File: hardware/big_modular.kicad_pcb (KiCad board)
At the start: 2 copper layers, 100.5 x 60 mm, 5 parts, among them J1 USB4105-GF-A

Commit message: WIP: consolidate PD-only Eurorack circuit on one sheet and dimension 2HP assembly
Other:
- board text added: "2 machined corner blocks: see ../docs/assembly.svg"
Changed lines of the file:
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@@
-	(footprint ""
-		(layer "F.Cu")
-		(at 80.75 52.275)
-		(property "Reference" "H3"
-			(at 0 0 0)
-			(layer "F.SilkS")
-			(hide yes)
-			(effects
-				(font
-					(size 1.27 1.27)
-				)
-			)
-		)
-		(property "Value" "MECHANICAL_NPTH"
-			(at 0 0 0)
-			(layer "F.Fab")
-			(hide yes)
-			(effects
-				(font
-					(size 1.27 1.27)
-				)
-			)
-		)
-		(property "Datasheet" ""
-			(at 0 0 0)
-			(layer "F.Fab")
-			(hide yes)
-			(effects
-				(font
-					(size 1.27 1.27)
-				)
-			)
-		)
-		(property "Description" ""
-			(at 0 0 0)
-			(layer "F.Fab")
-			(hide yes)
-			(effects
-				(font
-					(size 1.27 1.27)
-				)
-			)
-		)
-		(duplicate_pad_numbers_are_jumpers no)
-		(pad "" np_thru_hole circle
-			(at 0 0)
-			(size 2.2 2.2)
-			(drill 2.2)
-			(layers "*.Cu")
-		)
-		(embedded_fonts no)
-	)
-	(footprint ""
-		(layer "F.Cu")
-		(at 119.25 98.275)
-		(property "Reference" "H2"
-			(at 0 0 0)
-			(layer "F.SilkS")
-			(hide yes)
-			(effects
-				(font
-					(size 1.27 1.27)
-				)
-			)
-		)
-		(property "Value" "MECHANICAL_NPTH"
-			(at 0 0 0)
-			(layer "F.Fab")
-			(hide yes)
-			(effects
-				(font
-					(size 1.27 1.27)
-				)
-			)
-		)
-		(property "Datasheet" ""
-			(at 0 0 0)
-			(layer "F.Fab")
-			(hide yes)
-			(effects
-				(font
-					(size 1.27 1.27)
-				)
-			)
-		)
-		(property "Description" ""
-			(at 0 0 0)
-			(layer "F.Fab")
-			(hide yes)
-			(effects
-				(font
-					(size 1.27 1.27)
-				)
-			)
-		)
-		(duplicate_pad_numbers_are_jumpers no)
-		(pad "" np_thru_hole circle
-			(at 0 0)
-			(size 2.2 2.2)
-			(drill 2.2)
-			(layers "*.Cu")
-		)
-		(embedded_fonts no)
-	)
 	(footprint ""
 		(layer "F.Cu")
@@
 	(footprint ""
 		(layer "F.Cu")
-		(at 119.25 52.275)
-		(property "Reference" "H4"
+		(at 80.75 52.275)
+		(property "Reference" "H3"
 			(at 0 0 0)
 			(layer "F.SilkS")
@@
 		(embedded_fonts no)
 	)
+	(footprint ""
+		(layer "F.Cu")
+		(at 119.25 52.275)
+		(property "Reference" "H4"
+			(at 0 0 0)
+			(layer "F.SilkS")
+			(hide yes)
+			(effects
+				(font
+					(size 1.27 1.27)
+				)
+			)
+		)
+		(property "Value" "MECHANICAL_NPTH"
+			(at 0 0 0)
+			(layer "F.Fab")
+			(hide yes)
+			(effects
+				(font
+					(size 1.27 1.27)
+				)
+			)
+		)
+		(property "Datasheet" ""
+			(at 0 0 0)
+			(layer "F.Fab")
+			(hide yes)
+			(effects
+				(font
+					(size 1.27 1.27)
+				)
+			)
+		)
+		(property "Description" ""
+			(at 0 0 0)
+			(layer "F.Fab")
+			(hide yes)
+			(effects
+				(font
+					(size 1.27 1.27)
+				)
+			)
+		)
+		(duplicate_pad_numbers_are_jumpers no)
+		(pad "" np_thru_hole circle
+			(at 0 0)
+			(size 2.2 2.2)
+			(drill 2.2)
+			(layers "*.Cu")
+		)
+		(embedded_fonts no)
+	)
+	(footprint ""
+		(layer "F.Cu")
+		(at 119.25 98.275)
+		(property "Reference" "H2"
+			(at 0 0 0)
+			(layer "F.SilkS")
+			(hide yes)
+			(effects
+				(font
+					(size 1.27 1.27)
+				)
+			)
+		)
+		(property "Value" "MECHANICAL_NPTH"
+			(at 0 0 0)
+			(layer "F.Fab")
+			(hide yes)
+			(effects
+				(font
+					(size 1.27 1.27)
+				)
+			)
+		)
+		(property "Datasheet" ""
+			(at 0 0 0)
+			(layer "F.Fab")
+			(hide yes)
+			(effects
+				(font
+					(size 1.27 1.27)
+				)
+			)
+		)
+		(property "Description" ""
+			(at 0 0 0)
+			(layer "F.Fab")
+			(hide yes)
+			(effects
+				(font
+					(size 1.27 1.27)
+				)
+			)
+		)
+		(duplicate_pad_numbers_are_jumpers no)
+		(pad "" np_thru_hole circle
+			(at 0 0)
+			(size 2.2 2.2)
+			(drill 2.2)
+			(layers "*.Cu")
+		)
+		(embedded_fonts no)
+	)
+	(gr_line
+		(start 76.75 94.275)
+		(end 76.75 102.675)
+		(stroke
+			(width 0.15)
+			(type default)
+		)
+		(layer "Dwgs.User")
+	)
+	(gr_line
+		(start 76.75 102.675)
+		(end 84.75 102.675)
+		(stroke
+			(width 0.15)
+			(type default)
+		)
+		(layer "Dwgs.User")
+	)
+	(gr_line
+		(start 84.75 94.275)
+		(end 76.75 94.275)
+		(stroke
+			(width 0.15)
+			(type default)
+		)
+		(layer "Dwgs.User")
+	)
+	(gr_line
+		(start 84.75 102.675)
+		(end 84.75 94.275)
+		(stroke
+			(width 0.15)
+			(type default)
+		)
+		(layer "Dwgs.User")
+	)
 	(gr_line
 		(start 100 93)
@@
 		(start 100 101)
 		(end 100 93)
+		(stroke
+			(width 0.15)
+			(type default)
+		)
+		(layer "Dwgs.User")
+	)
+	(gr_line
+		(start 115.25 94.275)
+		(end 115.25 102.675)
+		(stroke
+			(width 0.15)
+			(type default)
+		)
+		(layer "Dwgs.User")
+	)
+	(gr_line
+		(start 115.25 102.675)
+		(end 123.25 102.675)
+		(stroke
+			(width 0.15)
+			(type default)
+		)
+		(layer "Dwgs.User")
+	)
+	(gr_line
+		(start 123.25 94.275)
+		(end 115.25 94.275)
+		(stroke
+			(width 0.15)
+			(type default)
+		)
+		(layer "Dwgs.User")
+	)
+	(gr_line
+		(start 123.25 102.675)
+		(end 123.25 94.275)
 		(stroke
 			(width 0.15)
@@
 		(layer "Dwgs.User")
 		(effects
+			(font
+				(size 0.9 0.9)
+				(thickness 0.12)
+			)
+		)
+	)
+	(gr_text "2 machined corner blocks: see ../docs/assembly.svg"
+		(at 100 117 0)
+		(layer "Dwgs.User")
+		(effects

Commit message: Update on the PCB.
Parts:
- added D10: 3mm THT LED / FORM 90 DEG, BigModular:LED_D3.0mm_Horizontal_O1.27mm_Z2.0mm_Edge, F.Cu at (72.5, 97.9)
- added J7: EURORACK OUTPUT PIGTAIL / NOT INPUT, BigModular:WireLanding_2x08_P2.54mm, F.Cu at (83.8, 77.3)
- added R32: 2.2k PROVISIONAL, BigModular:R_Axial_DIN0207_L6.3mm_D2.5mm_P7.62mm_Horizontal, F.Cu at (78.8, 90.3)
- added SW1: TL3340AF160QG, BigModular:SW_TL3340AF160QG_HandSolder, F.Cu at (126.8, 100.2)
- moved H4 28.2 mm to (106.2, 77.3)
- moved H3 25.0 mm to (79.2, 77.3)
- moved H1 24.7 mm to (57.8, 89.3)
- moved H2 24.7 mm to (142.2, 89.3)
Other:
- board size 100.5 x 60 mm -> 100.5 x 30 mm
- board text added: "1 / -12V / RED"
- board text added: "A4.2 / MAIN PCB / TWO-BOARD PLACEMENT / NO ROUTING"
- board text added: "J7 -> J2 OUTPUT ONLY"
- board text added: "M3 ONLY: two bracket holes; no standoffs / no board-to-board headers"
- board text added: "PWR K"
- board text added: "R32"
- board text added: "RESET"
- board text added: "UI nets isolated; not a working reset/power indicator circuit"
- board text added: "USB + 3mm THT LED + hand-solder 90-degree SMT reset; no middle board"
- board text removed: "2 machined corner blocks: see ../docs/assembly.svg"
- board text removed: "Carrier top X=3.170; PCB bottom X=1.570"
- board text removed: "Carrier: Y=14..114.5; Z=2..62 mm"
- board text removed: "J1 MOUTH Z=+0.800 / insertion +Z / panel normal"
- board text removed: "PLACEMENT ONLY / NO ROUTING / NOT BUILDABLE"

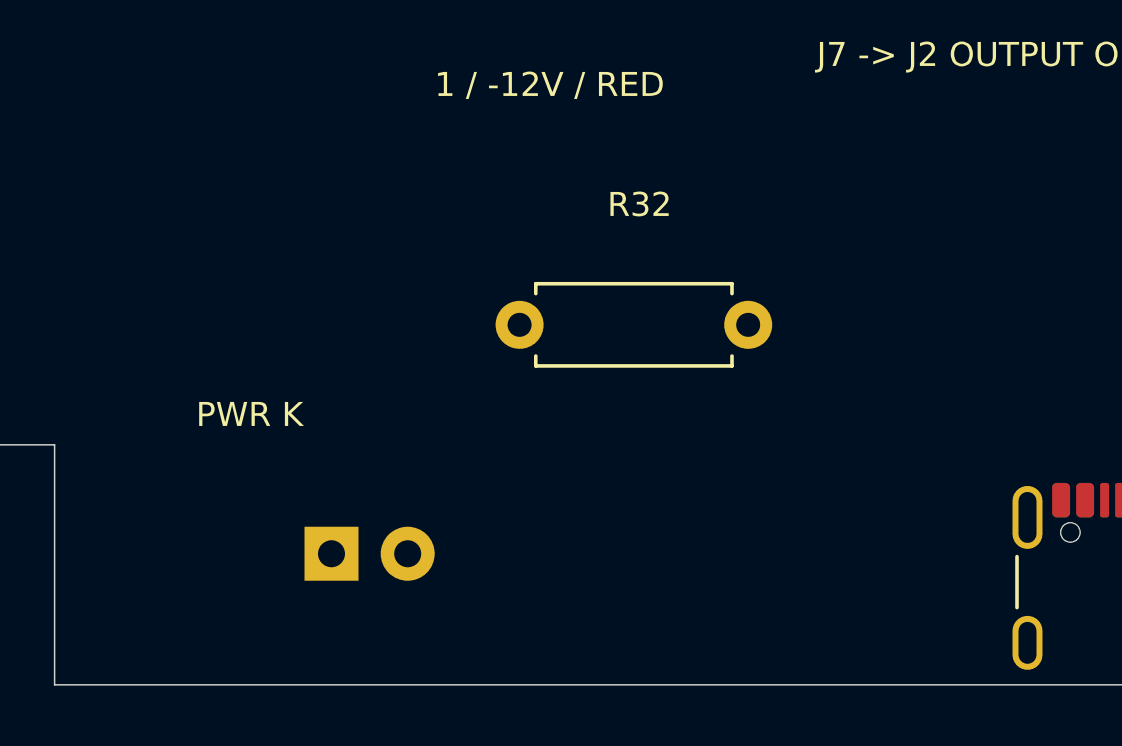
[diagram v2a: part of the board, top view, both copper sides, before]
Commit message: Save 9 V power-supply schematic prototype and LED mechanical provisions
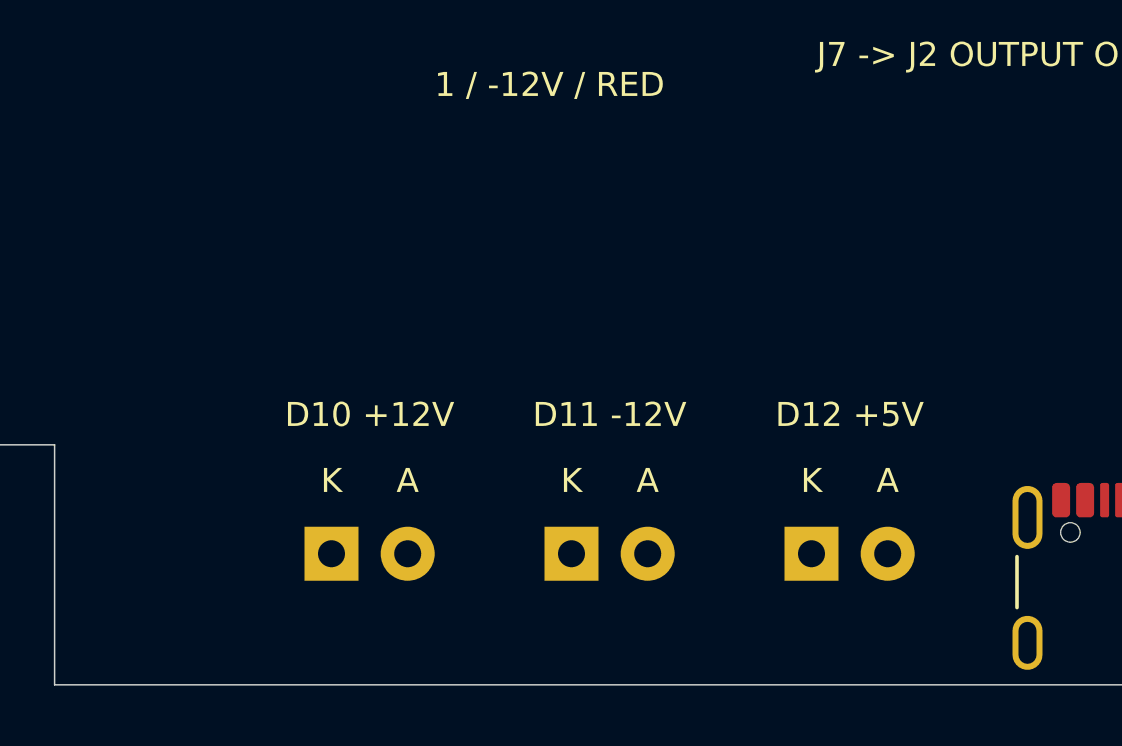
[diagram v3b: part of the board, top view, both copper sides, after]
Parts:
- removed R32: 2.2k PROVISIONAL, BigModular:R_Axial_DIN0207_L6.3mm_D2.5mm_P7.62mm_Horizontal
- added D11: RED 3mm / -12V / MANUAL, BigModular:LED_D3.0mm_Horizontal_O1.27mm_Z2.0mm_Edge, F.Cu at (80.5, 97.9)
- added D12: RED 3mm / +5V / MANUAL, BigModular:LED_D3.0mm_Horizontal_O1.27mm_Z2.0mm_Edge, F.Cu at (88.5, 97.9)
- D10: value 3mm THT LED / FORM 90 DEG -> RED 3mm / +12V / MANUAL
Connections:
- net UI_GND_PENDING renamed D10_K_PENDING
- D10 pad 2: LED_A_PENDING -> D10_A_PENDING
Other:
- board text added: "A"
- board text added: "D10 +12V"
- board text added: "D11 -12V"
- board text added: "D12 +5V"
- board text added: "K"
- board text added: "USB + 3 RED 3mm THT LEDs + hand-solder SMT reset; no middle board"
- board text removed: "PWR K"
- board text removed: "R32"
- board text removed: "USB + 3mm THT LED + hand-solder 90-degree SMT reset; no middle board"

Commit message: Replace MCU diagnostics with optional rail-sense IDC and single 5 V power LED
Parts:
- removed D11: RED 3mm / -12V / MANUAL, BigModular:LED_D3.0mm_Horizontal_O1.27mm_Z2.0mm_Edge
- removed D12: RED 3mm / +5V / MANUAL, BigModular:LED_D3.0mm_Horizontal_O1.27mm_Z2.0mm_Edge
- D10: value RED 3mm / +12V / MANUAL -> RED 3mm / +5V POWER / MANUAL
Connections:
- net D10_A_PENDING renamed LED_P_A
- D10 pad 1: D10_K_PENDING -> GND
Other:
- board text added: "D10 +5V POWER"
- board text added: "D10: final +5V via1k to anode; cathode GND; no routing"
- board text added: "USB + 1 RED 3mm THT +5V power LED + hand-solder SMT reset; no middle board"
- board text removed: "D10 +12V"
- board text removed: "D11 -12V"
- board text removed: "D12 +5V"
- board text removed: "UI nets isolated; not a working reset/power indicator circuit"
- board text removed: "USB + 3 RED 3mm THT LEDs + hand-solder SMT reset; no middle board"

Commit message: Move USB, retry button and power LED to top; synchronize 64 V1 footprints without routing
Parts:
- added C1: 1u 50V X7R, BigModular:C_0805_2012Metric, F.Cu at (170.0, 75.0)
- added C10: 6.8p 50V C0G, BigModular:C_0603_1608Metric, F.Cu at (188.0, 75.0)
- added C11: 6.8p 50V C0G, BigModular:C_0603_1608Metric, F.Cu at (206.0, 75.0)
- added C12: 220n 50V X7R, BigModular:C_0603_1608Metric, F.Cu at (224.0, 75.0)
- added C13: 10n 50V X7R, BigModular:C_0603_1608Metric, F.Cu at (242.0, 75.0)
- added C14: 4.7n 50V C0G, BigModular:C_0603_1608Metric, F.Cu at (260.0, 75.0)
- added C15: 100n 50V X7R, BigModular:C_0603_1608Metric, F.Cu at (278.0, 75.0)
- added C16: 10u 25V X7R, BigModular:C_1206_3216Metric, F.Cu at (296.0, 75.0)
- added C17: 10u 25V X7R, BigModular:C_1206_3216Metric, F.Cu at (314.0, 75.0)
- added C18: 10u 25V X7R, BigModular:C_1206_3216Metric, F.Cu at (332.0, 75.0)
- added C19: 22u 25V X7R, BigModular:C_1210_3225Metric, F.Cu at (170.0, 93.0)
- added C2: 100n 50V X7R, BigModular:C_0603_1608Metric, F.Cu at (188.0, 93.0)
- added C20: 100n 50V X7R, BigModular:C_0603_1608Metric, F.Cu at (206.0, 93.0)
- added C3: 100n 50V X7R, BigModular:C_0603_1608Metric, F.Cu at (224.0, 93.0)
- added C35: 100n 50V X7R, BigModular:C_0603_1608Metric, F.Cu at (242.0, 93.0)
- added C36: 100n 50V X7R, BigModular:C_0603_1608Metric, F.Cu at (260.0, 93.0)
- added C37: 22u 25V X7R, BigModular:C_1210_3225Metric, F.Cu at (278.0, 93.0)
- added C38: 22u 25V X7R, BigModular:C_1210_3225Metric, F.Cu at (296.0, 93.0)
- added C4: 10u 25V X7R, BigModular:C_1206_3216Metric, F.Cu at (314.0, 93.0)
- added C5: 10u 25V X7R, BigModular:C_1206_3216Metric, F.Cu at (332.0, 93.0)
- added C6: 22u 25V X7R, BigModular:C_1210_3225Metric, F.Cu at (170.0, 111.0)
- added C7: 100n 50V X7R, BigModular:C_0603_1608Metric, F.Cu at (188.0, 111.0)
- added C8: 22u 25V X7R, BigModular:C_1210_3225Metric, F.Cu at (206.0, 111.0)
- added C9: 22u 25V X7R, BigModular:C_1210_3225Metric, F.Cu at (224.0, 111.0)
- added D2: SS34 40V, BigModular:D_SMA, F.Cu at (242.0, 111.0)
- added D3: SS34 40V, BigModular:D_SMA, F.Cu at (260.0, 111.0)
- added F1: 3A 32V candidate, BigModular:Fuse_1206_3216Metric, F.Cu at (278.0, 111.0)
- added L1: 6.8uH 20% shielded, BigModular:L_KOHER_MDA1040, F.Cu at (296.0, 111.0)
- added L2: 4.7uH 20% shielded, BigModular:L_CENKER_CKCS6045, F.Cu at (314.0, 111.0)
- added L3: 4.7uH 20% shielded, BigModular:L_CENKER_CKCS6045, F.Cu at (332.0, 111.0)
- added L4: 6.8uH 20% shielded, BigModular:L_KOHER_MDA1040, F.Cu at (170.0, 129.0)
- added R10: 12.9k 0.1%, BigModular:R_0603_1608Metric, F.Cu at (188.0, 129.0)
- added R12: 1.33M 1%, BigModular:R_0603_1608Metric, F.Cu at (206.0, 129.0)
- added R13: 150k 1%, BigModular:R_0603_1608Metric, F.Cu at (224.0, 129.0)
- added R14: 1.33M 1%, BigModular:R_0603_1608Metric, F.Cu at (242.0, 129.0)
- added R15: 150k 1%, BigModular:R_0603_1608Metric, F.Cu at (260.0, 129.0)
- added R16: 100 1%, BigModular:R_0603_1608Metric, F.Cu at (278.0, 129.0)
- added R17: 100k 1%, BigModular:R_0603_1608Metric, F.Cu at (296.0, 129.0)
- added R18: 13.5k 0.1%, BigModular:R_0603_1608Metric, F.Cu at (314.0, 129.0)
- added R2: 6.8k 1%, BigModular:R_0603_1608Metric, F.Cu at (332.0, 129.0)
- added R25: 10k 1%, BigModular:R_0603_1608Metric, F.Cu at (170.0, 147.0)
- added R26: 10k 1%, BigModular:R_0603_1608Metric, F.Cu at (188.0, 147.0)
- added R27: 10k 1%, BigModular:R_0603_1608Metric, F.Cu at (206.0, 147.0)
- added R31: 10k 1%, BigModular:R_0603_1608Metric, F.Cu at (224.0, 147.0)
- added R32: 1k 1%, BigModular:R_0603_1608Metric, F.Cu at (242.0, 147.0)
- added R36: 402k 1%, BigModular:R_0603_1608Metric, F.Cu at (260.0, 147.0)
- added R38: 100k 1%, BigModular:R_0603_1608Metric, F.Cu at (278.0, 147.0)
- added R4: 562k 1%, BigModular:R_0603_1608Metric, F.Cu at (296.0, 147.0)
- added R40: 100k 1%, BigModular:R_0603_1608Metric, F.Cu at (314.0, 147.0)
- added R5: 100k 1%, BigModular:R_0603_1608Metric, F.Cu at (332.0, 147.0)
- added R6: 806k 1%, BigModular:R_0603_1608Metric, F.Cu at (170.0, 165.0)
- added R60: 150k 1%, BigModular:R_0603_1608Metric, F.Cu at (188.0, 165.0)
- added R7: 100k 1%, BigModular:R_0603_1608Metric, F.Cu at (206.0, 165.0)
- added R8: 6.04k 1%, BigModular:R_0603_1608Metric, F.Cu at (224.0, 165.0)
- added R9: 100k 0.1%, BigModular:R_0603_1608Metric, F.Cu at (242.0, 165.0)
- added U1: CH224A, BigModular:SSOP-10-1EP_3.9x4.9mm_P1mm_EP2.1x3.3mm, F.Cu at (260.0, 165.0)
- added U2: TPS26600PWPR, BigModular:HTSSOP-16-1EP_4.4x5mm_P0.65mm_EP3.4x5mm_Mask2.66x2.46mm, F.Cu at (278.0, 165.0)
- added U3: TPS54302DDCR, BigModular:SOT-23-6, F.Cu at (296.0, 165.0)
- added U4: TPS65131RGER, BigModular:Texas_RGE0024B_VQFN-24-1EP_4x4mm_P0.5mm_EP2.45x2.45mm, F.Cu at (314.0, 165.0)
- added U5: TPS54302DDCR, BigModular:SOT-23-6, F.Cu at (332.0, 165.0)
- J7: value EURORACK OUTPUT PIGTAIL / NOT INPUT -> Manual IDC wire landing
- moved SW1 48.0 mm to (78.8, 100.2)
- moved J1 30.8 mm to (69.2, 99.8)
- moved D10 11.5 mm to (84.0, 97.9)
- renumbered H2 to ?, H3 to ?, H1 to ?, H4 to ?
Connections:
- net GND renamed /GND
- net N12 renamed /N12
- net P12 renamed /P12
- net P5 renamed /P5
- net RESET_A_PENDING renamed /Autonomous hardware window and retry/EF_SHDN
- net VBUS_RAW renamed /USB PD input/USB_VBUS
- D10 pad 2: LED_P_A -> /Board output and power LED/LED_P_A
- J1 pad A5: CC1 -> /USB PD input/CC1
- J1 pad A6: (no net) -> unconnected-(J1-D+-PadA6)
- J1 pad A7: (no net) -> unconnected-(J1-D--PadA7)
- J1 pad A8: (no net) -> unconnected-(J1-SBU1-PadA8)
- J1 pad B5: CC2 -> /USB PD input/CC2
- J1 pad B6: (no net) -> unconnected-(J1-D+-PadB6)
- J1 pad B7: (no net) -> unconnected-(J1-D--PadB7)
- J1 pad B8: (no net) -> unconnected-(J1-SBU2-PadB8)
- J7 pad 13: (no net) -> unconnected-(J7-Pin_13-Pad13)
- J7 pad 14: (no net) -> unconnected-(J7-Pin_14-Pad14)
- J7 pad 15: (no net) -> unconnected-(J7-Pin_15-Pad15)
- J7 pad 16: (no net) -> unconnected-(J7-Pin_16-Pad16)
- SW1 pad 2: RESET_B_PENDING -> /Autonomous hardware window and retry/RTN
- SW1 pad MP: (no net) -> unconnected-(SW1-CASE-PadMP)
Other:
- board text added: "J7 OUTPUT ONLY"
- board text added: "RETRY"
- board text added: "STAGED OFF-BOARD: 60 parts; place power circuits deliberately before routing"
- board text added: "V1 / 64 PARTS SYNCHRONIZED / NO ROUTING"
- board text removed: "A4.2 / MAIN PCB / TWO-BOARD PLACEMENT / NO ROUTING"
- board text removed: "J7 -> J2 OUTPUT ONLY"
- board text removed: "RESET"

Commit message: Swap retry switch and power LED positions on carrier and front panel
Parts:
- moved D10 6.50 mm to (77.5, 97.9)
- moved SW1 6.50 mm to (85.2, 100.2)
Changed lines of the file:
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@@
 		(locked yes)
 		(layer "F.Cu")
-		(at 78.75 100.175)
+		(at 85.25 100.175)
 		(descr "TL3340AF160QG, P021301 Rev B: hand-solder toe extensions, pin1+3 common; no substitution by size alone")
 		(property "Reference" "SW1"
@@
 		(locked yes)
 		(layer "F.Cu")
-		(at 83.98 97.905)
+		(at 77.48 97.905)
 		(descr "LED, diameter 3.0mm, horizontal offset 1.27mm, z-position of LED center 2.0mm, 2 pins, generated by kicad-footprint-generator")
 		(tags "LED")
@@
 		(layer "Edge.Cuts")
 	)
-	(gr_text "RETRY"
-		(at 78.75 92.275 0)
+	(gr_text "K"
+		(at 77.48 95.475 0)
 		(layer "F.SilkS")
 		(effects
@@
 		)
 	)
-	(gr_text "1 / -12V / RED"
-		(at 79.75 82.275 0)
+	(gr_text "D10 +5V POWER"
+		(at 78.75 93.275 0)
 		(layer "F.SilkS")
 		(effects
@@
 		)
 	)
-	(gr_text "K"
-		(at 83.98 95.475 0)
+	(gr_text "1 / -12V / RED"
+		(at 79.75 82.275 0)
 		(layer "F.SilkS")
 		(effects
@@
 		)
 	)
-	(gr_text "D10 +5V POWER"
-		(at 85.25 93.275 0)
+	(gr_text "A"
+		(at 80.02 95.475 0)
 		(layer "F.SilkS")
 		(effects
@@
 		)
 	)
-	(gr_text "A"
-		(at 86.52 95.475 0)
+	(gr_text "RETRY"
+		(at 85.25 92.275 0)
 		(layer "F.SilkS")
 		(effects

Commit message: Complete four-layer routing, adopt proven HRO USB-C and release checked fabrication files
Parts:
- J1: value USB4105-GF-A -> TYPE-C-31-M-12; footprint BigModular:USB_C_Receptacle_GCT_USB4105-xx-A_16P_TopMnt_Horizontal -> BigModular:HRO-TYPE-C-31-M-12
- moved R2 265.0 mm to (70.8, 84.5), turned to 180 degrees
- moved R5 262.3 mm to (77.0, 85.5), turned to 180 degrees
- moved U5 234.7 mm to (108.0, 95.0)
- moved C18 228.2 mm to (104.7, 95.0), turned to 90 degrees
- moved R4 228.1 mm to (76.8, 83.9)
- moved C4 224.2 mm to (90.0, 82.7)
- moved U2 210.7 mm to (82.5, 86.5)
- moved U4 207.7 mm to (124.0, 81.0)
- moved U1 205.0 mm to (69.3, 89.7)
- moved R18 204.1 mm to (112.2, 98.3), turned to 180 degrees
- moved C38 203.1 mm to (93.0, 87.0)
- moved F1 203.0 mm to (76.0, 90.5)
- moved C5 202.4 mm to (129.7, 97.5), turned to 90 degrees
- moved L3 201.1 mm to (132.6, 84.8)
- moved L2 199.4 mm to (117.0, 80.3)
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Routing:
- net /N12: track 0.00 -> 129.4 mm, vias 0 -> 7
- net /VPROT: track 0.00 -> 92.4 mm, vias 0 -> 10
- net /MID: track 0.00 -> 91.1 mm, vias 0 -> 8
- net /P5: track 0.00 -> 84.8 mm, vias 0 -> 10
- net /GND: track 0.00 -> 79.8 mm, vias 0 -> 49
- net /P12: track 0.00 -> 59.9 mm, vias 0 -> 6
- net /VIN9: track 0.00 -> 52.9 mm, vias 0 -> 11
- net /Autonomous hardware window and retry/RTN: track 0.00 -> 24.7 mm, vias 0 -> 12
- net /Autonomous hardware window and retry/EF_SHDN: track 0.00 -> 21.0 mm, vias 0 -> 3
- net /USB PD input/USB_VBUS: track 0.00 -> 20.6 mm, vias 0 -> 3
- net /Direct bipolar rails/NEG_FB: track 0.00 -> 14.1 mm, vias 0 -> 2
- net /Direct bipolar rails/INV_SW: track 0.00 -> 12.4 mm
- net /Autonomous hardware window and retry/EF_MODE: track 0.00 -> 11.5 mm, vias 0 -> 2
- net /Direct bipolar rails/BI_EN: track 0.00 -> 11.5 mm, vias 0 -> 2
- net /USB PD input/CC1: track 0.00 -> 11.3 mm
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- added copper zone on B.Cu, net /Autonomous hardware window and retry/RTN
- added copper zone on F.Cu, net /Autonomous hardware window and retry/RTN
- added copper zone on In2.Cu, net /Autonomous hardware window and retry/RTN
- added copper zone on In1.Cu, net /GND
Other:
- copper layers 2 -> 4
- board text added: "64 PLACED / HRO USB-C / BARE-PCB ARTWORK - SEE FABRICATION NOTES"
- board text added: "D10: final +5V via 1k; cathode GND; source schematic unchanged"
- board text added: "V1 / HRO / FOUR-LAYER ROUTED CARRIER"
- board text removed: "D10: final +5V via1k to anode; cathode GND; no routing"
- board text removed: "STAGED OFF-BOARD: 60 parts; place power circuits deliberately before routing"
- board text removed: "V1 / 64 PARTS SYNCHRONIZED / NO ROUTING"
